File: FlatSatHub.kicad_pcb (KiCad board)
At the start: 4 copper layers, 166.3 x 166.3 mm, 38 parts, among them J1 Jack-DC, J10 DB26_Male_HighDensity_Mountin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, J11 HEADER_4x2, J12 DB26_Male_HighDensity_Mountin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, J13 HEADER_4x2, J14 DB26_Male_HighDensity_Mountin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, J15 DB26_Male_HighDensity_Mountin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, J16 DB26_Male_HighDensity_Mountin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, J2 HEADER_4x2, J3 HEADER_4x2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

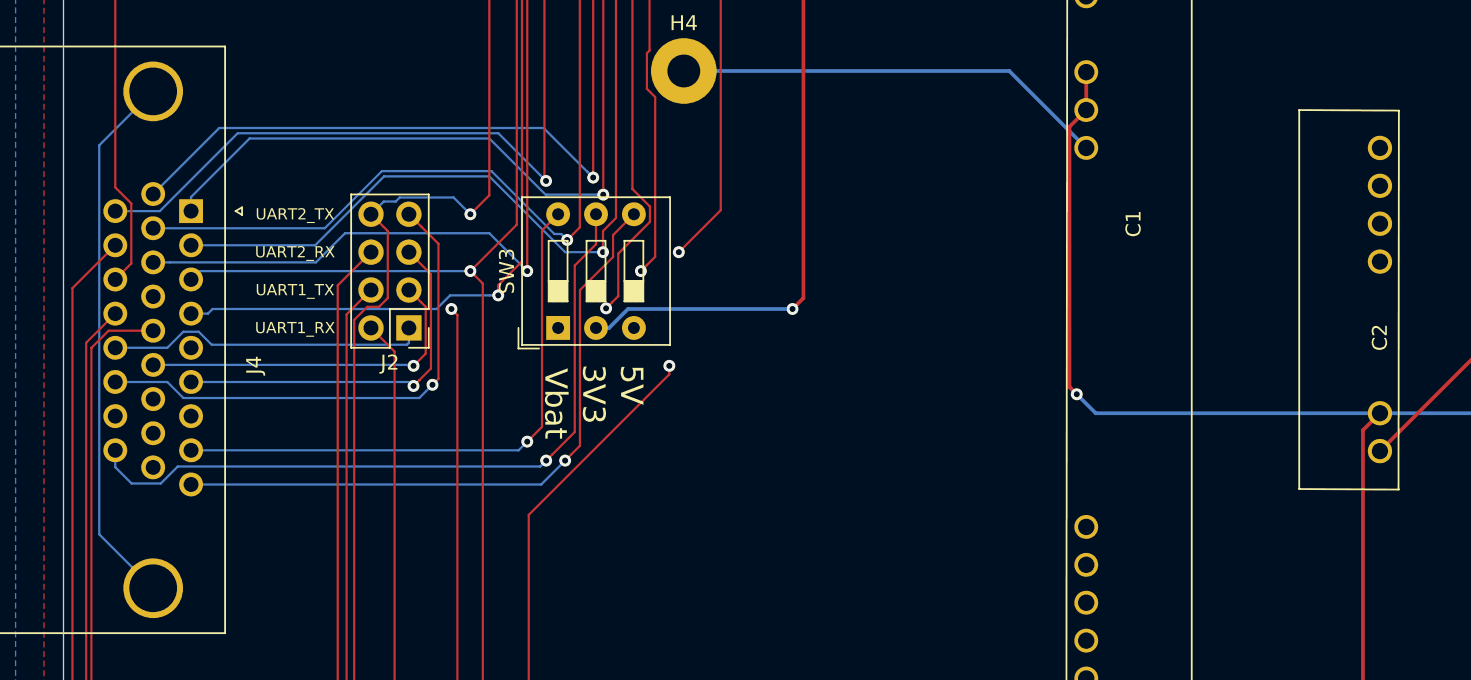
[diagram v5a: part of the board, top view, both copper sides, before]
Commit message: fix dc converter wiring and gnd track size
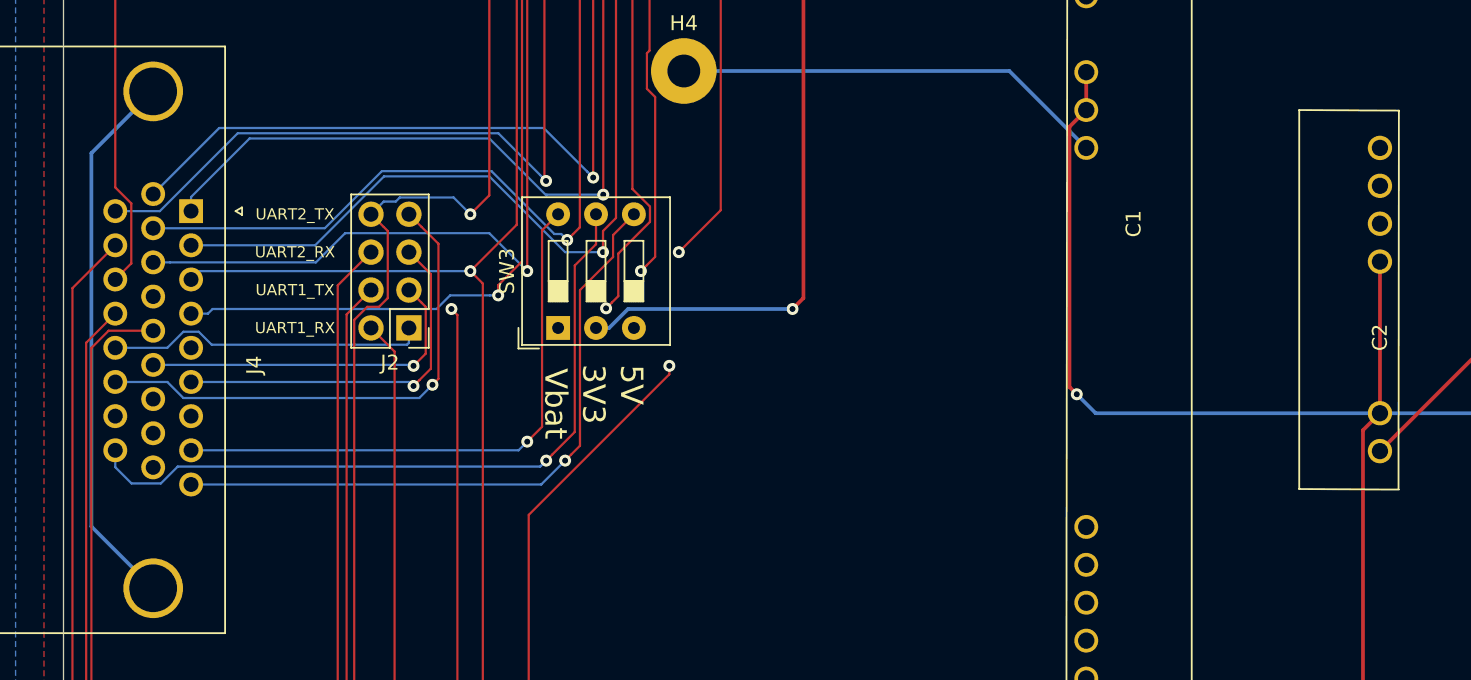
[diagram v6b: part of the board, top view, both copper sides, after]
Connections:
- C2 pad 4: Net-(C2-Pad4) -> /Vin
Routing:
- net /Vin: track 149.2 -> 159.4 mm

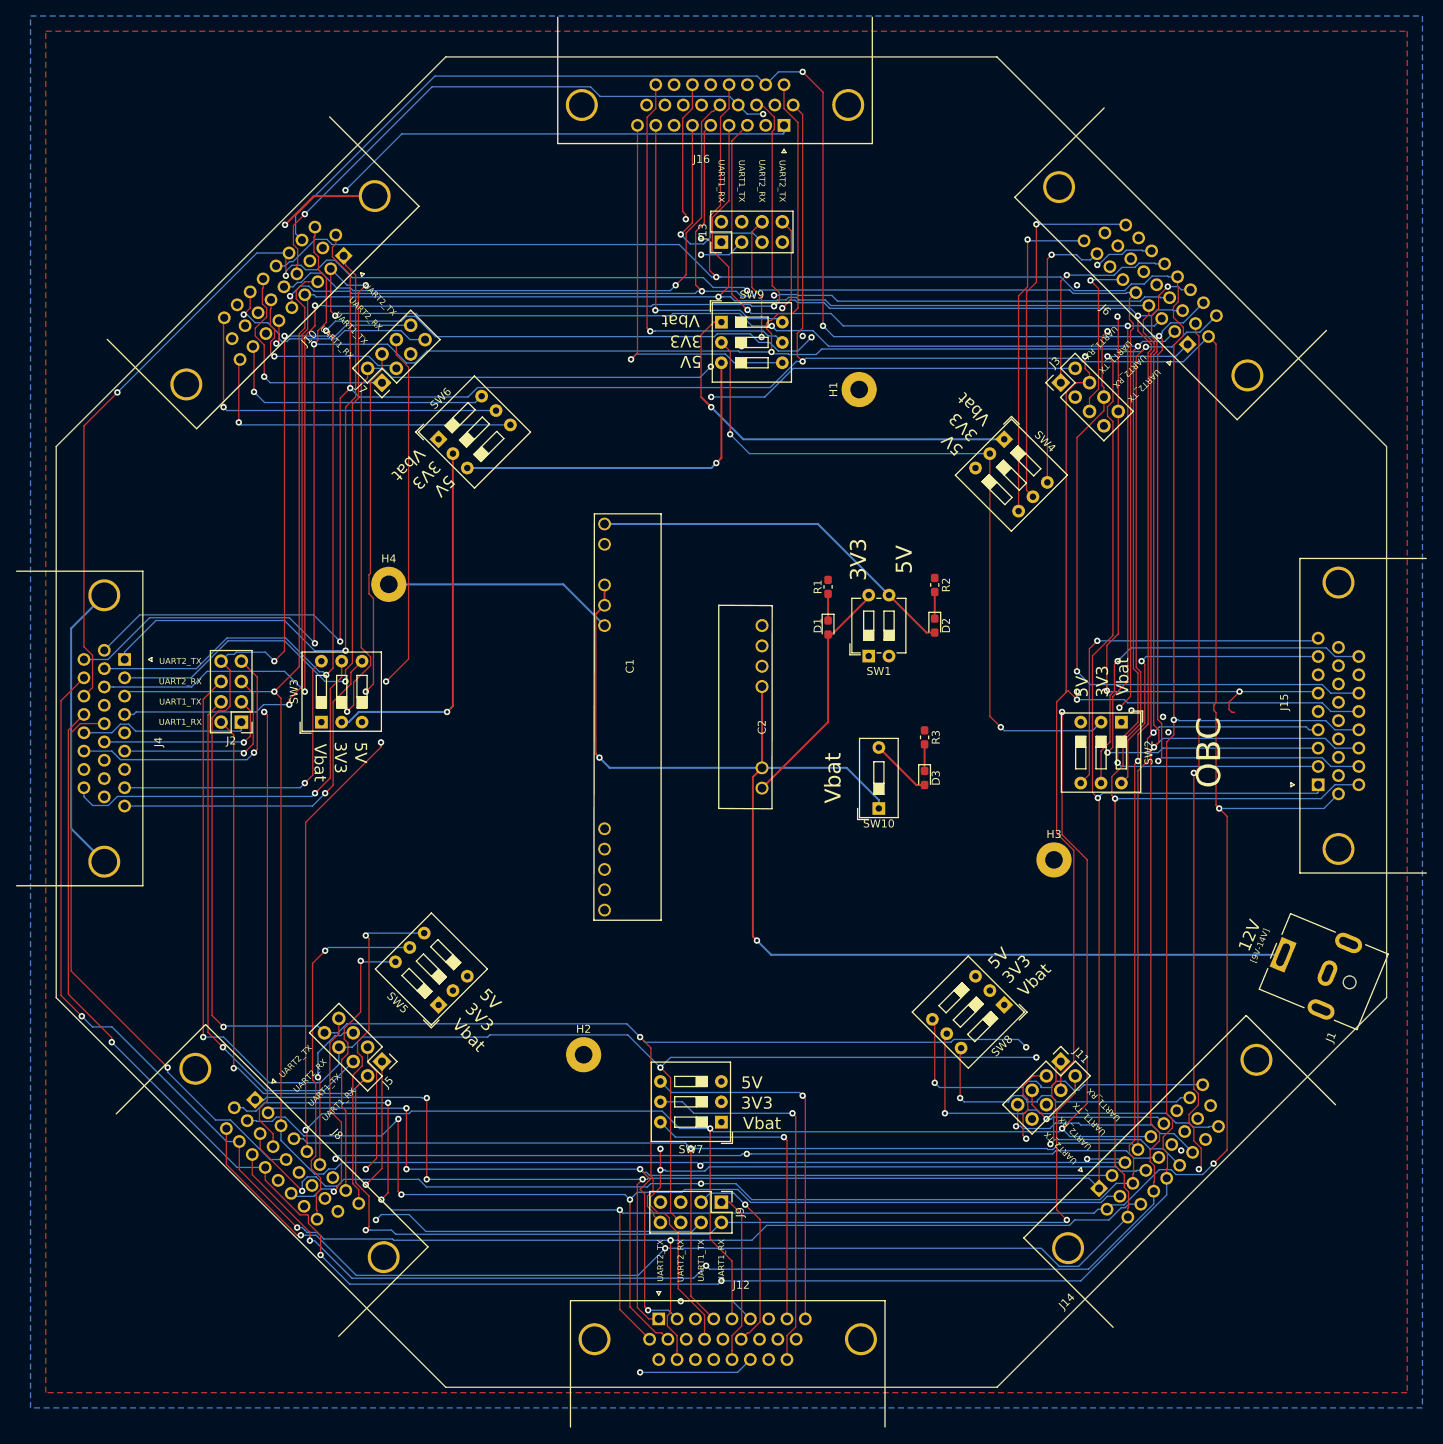
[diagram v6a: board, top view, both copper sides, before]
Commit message: moved vias out of the way of writings
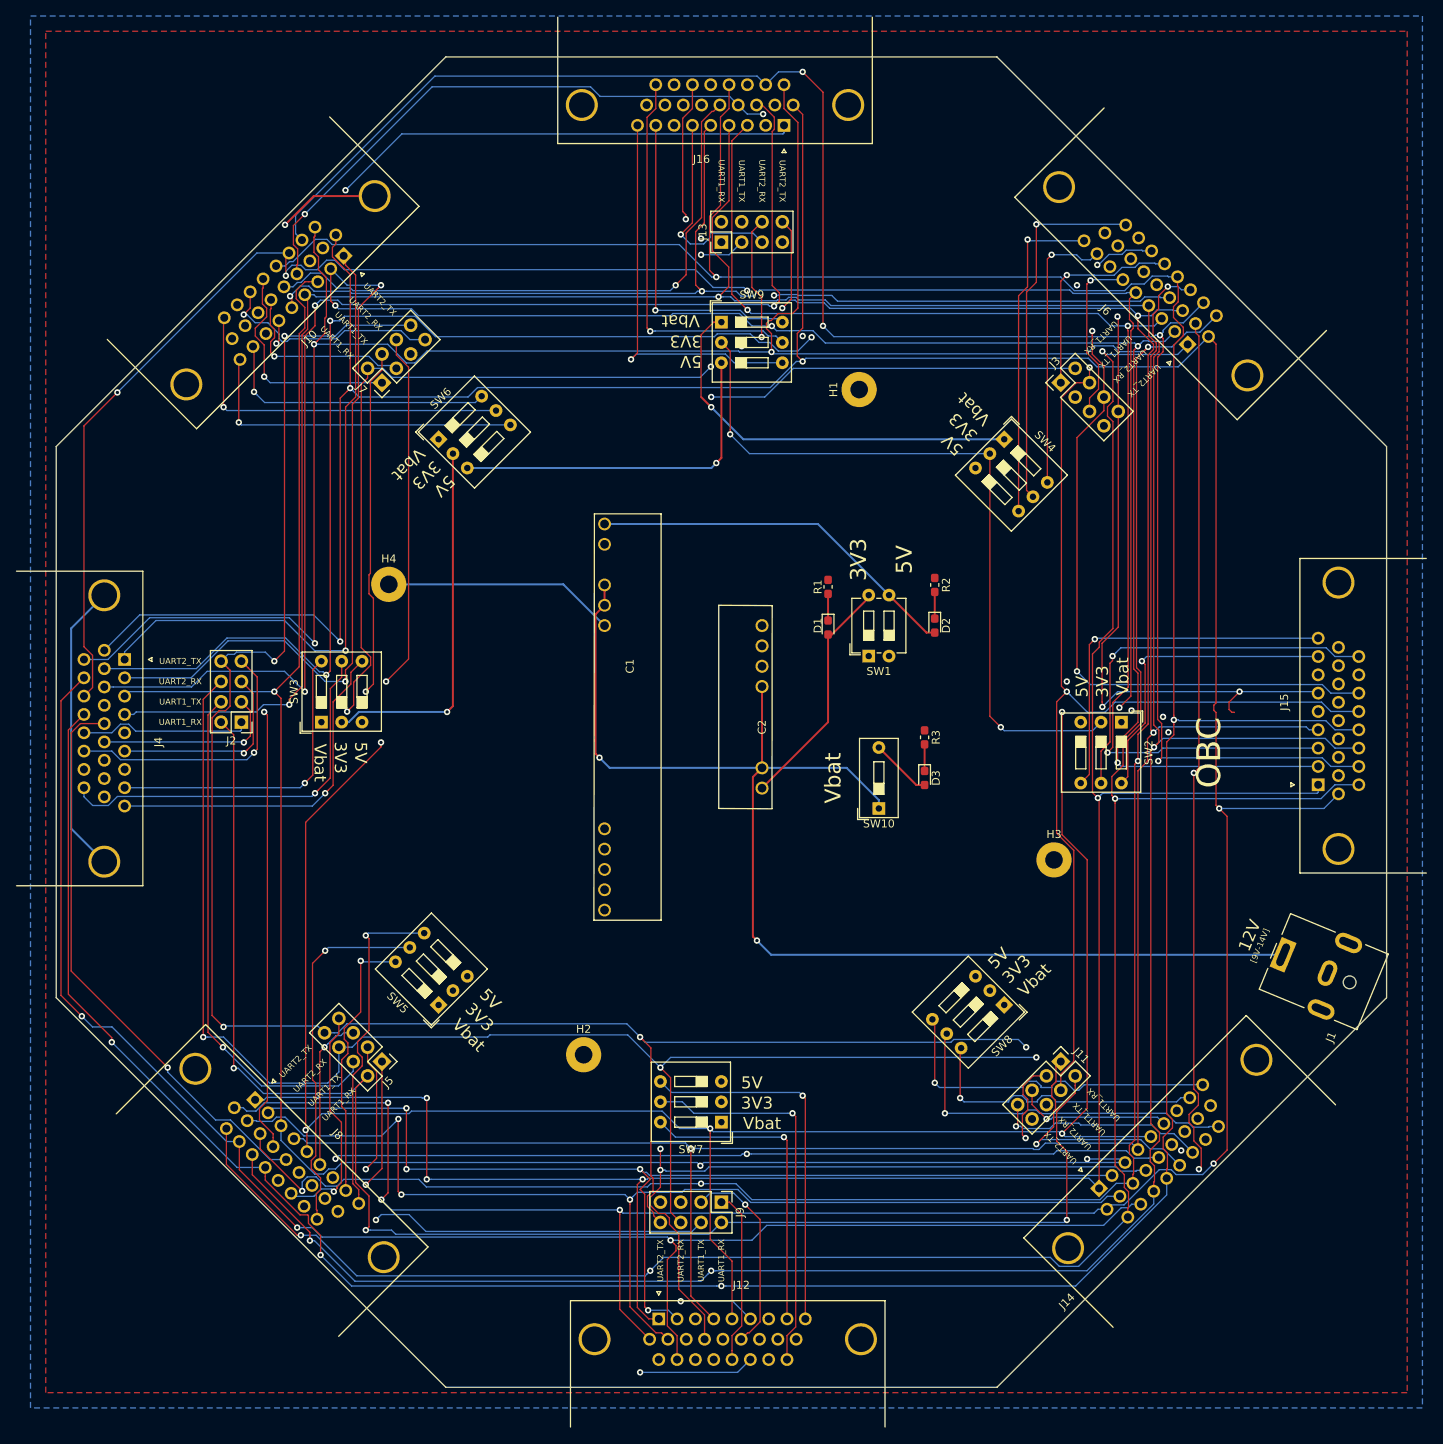
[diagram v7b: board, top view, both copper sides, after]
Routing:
- net OBC_UART2_RX: track 430.0 -> 433.6 mm
- net /I2C1_SCL: track 525.3 -> 522.7 mm
- net /sheet5F237BCE/UART1_RX: track 29.0 -> 31.4 mm
- net /SPI1_MISO: track 495.3 -> 497.0 mm
- net /SPI1_SCK: track 512.3 -> 510.9 mm
- net OBC_UART1_RX: track 430.7 -> 432.0 mm
- net OBC_UART2_TX: track 438.0 -> 437.0 mm
- net /Sheet5F2C117D/bus_3v3: track 47.4 -> 48.1 mm
- net /I2C2_SCL: track 503.2 -> 503.9 mm
- net /SPI1_MOSI: track 492.8 -> 493.4 mm
- net /sheet5F22D1E8/UART2_TX: track 28.4 -> 29.0 mm
- net /I2C1_SDA: track 508.2 -> 508.7 mm
- net /I2C2_SDA: track 498.4 -> 499.0 mm
